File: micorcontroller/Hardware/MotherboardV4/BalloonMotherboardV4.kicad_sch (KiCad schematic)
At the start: 6 parts

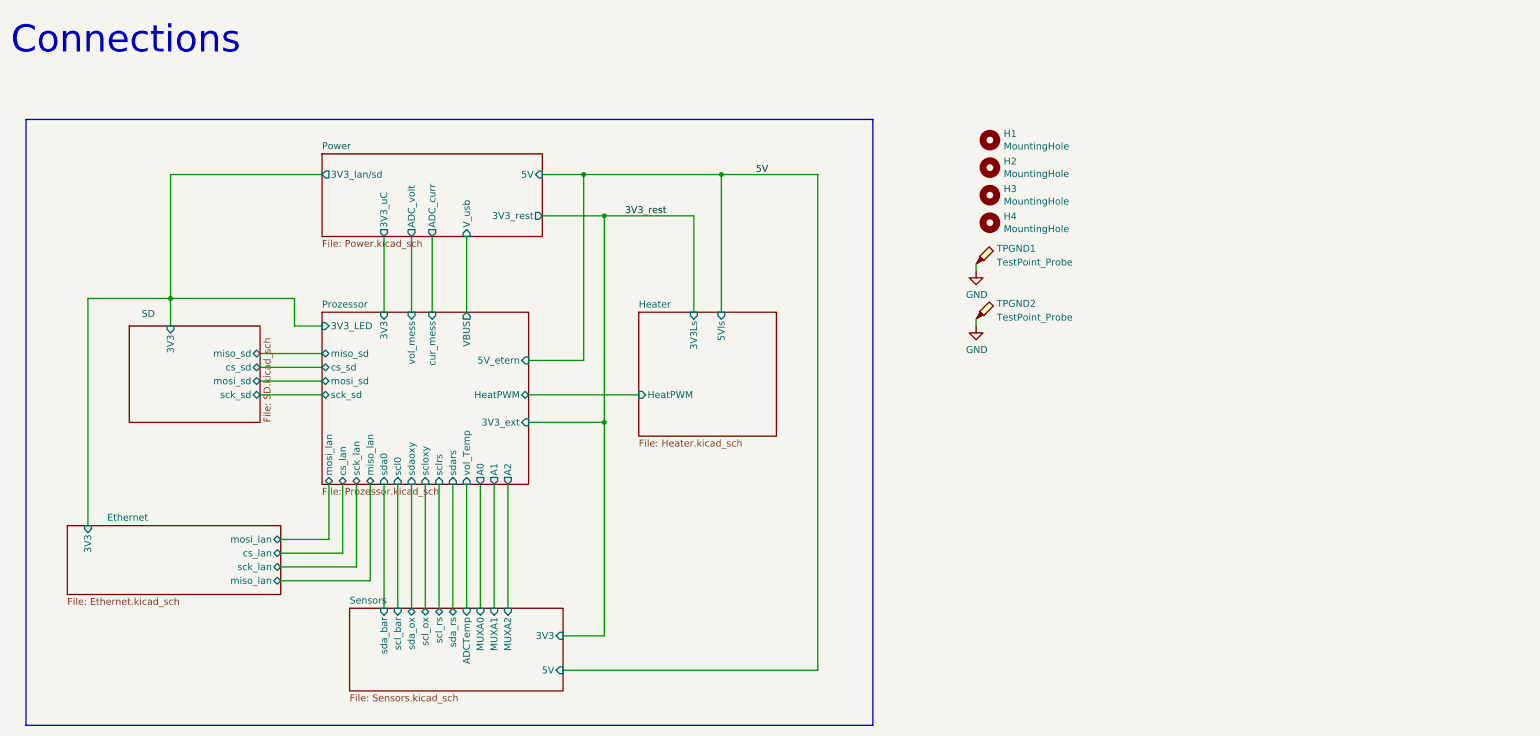
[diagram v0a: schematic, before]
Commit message: added NTC calculation
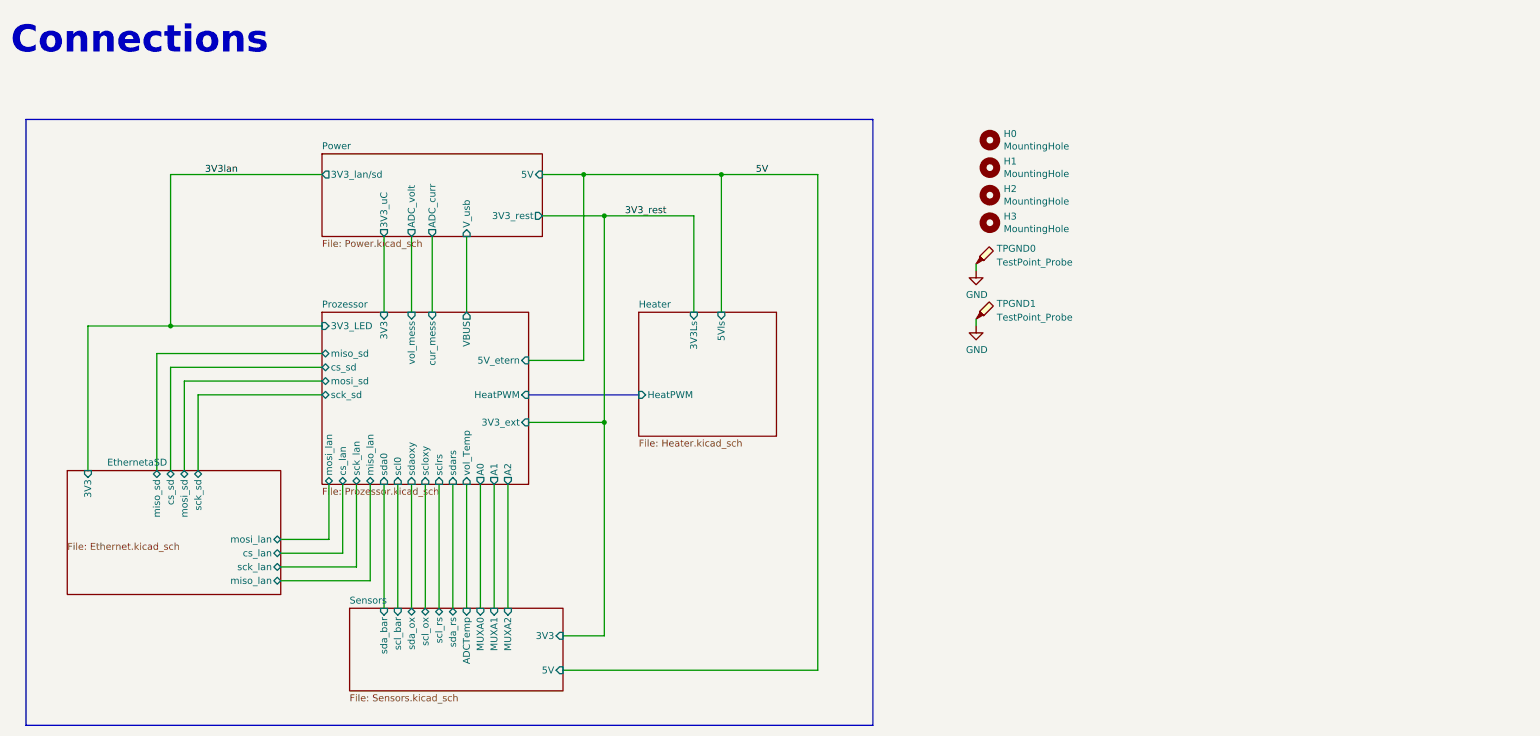
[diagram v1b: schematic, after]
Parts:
- renumbered H1 to H0, H2 to H1, H3 to H2, H4 to H3, TPGND1 to TPGND0, TPGND2 to TPGND1
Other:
- sheet Ethernet renamed EthernetaSD
- removed sheet SD
- sheet EthernetaSD ports: added cs_sd, miso_sd, mosi_sd, sck_sd; removed none

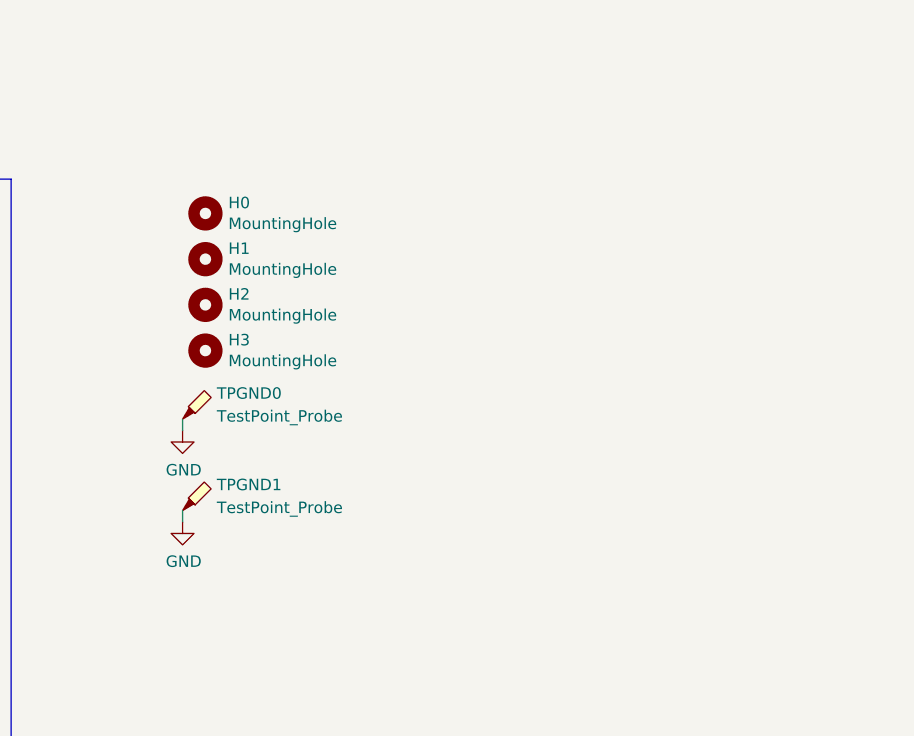
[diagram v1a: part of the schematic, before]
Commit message: added a serial command field for easy debugging
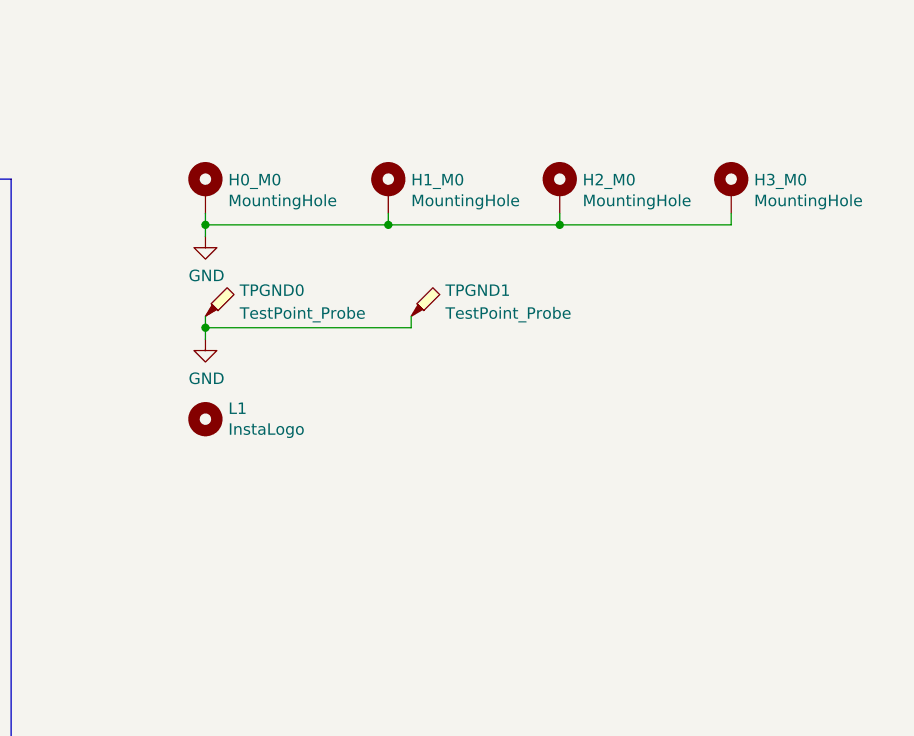
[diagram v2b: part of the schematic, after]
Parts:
- added L1: InstaLogo, SamacSys_Parts:insta, symbol Mechanical:MountingHole
- H0_M0: renamed from H0; symbol Mechanical:MountingHole -> Mechanical:MountingHole_Pad
- H1_M0: renamed from H1; symbol Mechanical:MountingHole -> Mechanical:MountingHole_Pad
- H2_M0: renamed from H2; symbol Mechanical:MountingHole -> Mechanical:MountingHole_Pad
- H3_M0: renamed from H3; symbol Mechanical:MountingHole -> Mechanical:MountingHole_Pad
- TPGND0, TPGND1: now left out of the parts list
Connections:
- net GND: now also H0_M0.1, H1_M0.1, H2_M0.1, H3_M0.1
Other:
- moved on the sheet: TPGND0, TPGND1

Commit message: Switch to header BASED C file system {headache incomming}
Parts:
- renumbered L1 to L0
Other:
- sheet Power ports: added VBUCK; removed none
- sheet Sensors ports: added 3V3uC, BUCK; removed none
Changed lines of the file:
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@@
+	)
+	(junction
+		(at 91.44 66.04)
+		(diameter 0)
+		(color 0 0 0 0)
 	)
 	(junction
@@
 	(wire
 		(pts
+			(xy 120.65 52.07) (xy 167.64 52.07)
+		)
+		(stroke
+			(width 0)
+			(type default)
+		)
+	)
+	(wire
+		(pts
 			(xy 203.2 53.34) (xy 203.2 54.61)
 		)
@@
 	(wire
 		(pts
+			(xy 167.64 52.07) (xy 167.64 135.89)
+		)
+		(stroke
+			(width 0)
+			(type default)
+		)
+	)
+	(wire
+		(pts
 			(xy 57.15 88.9) (xy 80.01 88.9)
 		)
@@
 	(wire
 		(pts
+			(xy 125.73 130.81) (xy 125.73 66.04)
+		)
+		(stroke
+			(width 0)
+			(type default)
+		)
+	)
+	(wire
+		(pts
 			(xy 49.53 81.28) (xy 49.53 102.87)
 		)
@@
 	(wire
 		(pts
+			(xy 91.44 66.04) (xy 91.44 73.66)
+		)
+		(stroke
+			(width 0)
+			(type default)
+		)
+	)
+	(wire
+		(pts
 			(xy 104.14 105.41) (xy 104.14 128.27)
 		)
@@
 	(wire
 		(pts
+			(xy 124.46 130.81) (xy 125.73 130.81)
+		)
+		(stroke
+			(width 0)
+			(type default)
+		)
+	)
+	(wire
+		(pts
 			(xy 118.11 93.98) (xy 132.08 93.98)
 		)
@@
 	(wire
 		(pts
+			(xy 125.73 66.04) (xy 91.44 66.04)
+		)
+		(stroke
+			(width 0)
+			(type default)
+		)
+	)
+	(wire
+		(pts
 			(xy 132.08 55.88) (xy 148.59 55.88)
 		)
@@
 	(wire
 		(pts
+			(xy 167.64 135.89) (xy 124.46 135.89)
+		)
+		(stroke
+			(width 0)
+			(type default)
+		)
+	)
+	(wire
+		(pts
 			(xy 226.06 54.61) (xy 226.06 53.34)
 		)
@@
 	(wire
 		(pts
-			(xy 91.44 59.69) (xy 91.44 73.66)
+			(xy 91.44 59.69) (xy 91.44 66.04)
 		)
 		(stroke
@@
 		(on_board yes)
 		(dnp no)
-		(property "Reference" "L1"
+		(property "Reference" "L0"
 			(at 205.74 63.6016 0)
 			(effects
@@
 			(project "BalloonMotherboardV4"
 				(path "/a70d325c-f83f-4714-a2b6-4ef8919d016e"
-					(reference "L1")
+					(reference "L0")
 					(unit 1)
 				)
@@
 		(on_board yes)
 		(dnp no)
-		(property "Reference" "#PWR00"
+		(property "Reference" "#PWR01"
 			(at 203.2 62.23 0)
 			(effects
@@
 			(project "BalloonMotherboardV4"
 				(path "/a70d325c-f83f-4714-a2b6-4ef8919d016e"
-					(reference "#PWR00")
+					(reference "#PWR01")
 					(unit 1)
 				)
@@
 		(on_board yes)
 		(dnp no)
-		(property "Reference" "#PWR01"
+		(property "Reference" "#PWR00"
 			(at 203.2 50.8 0)
 			(effects
@@
 			(project "BalloonMotherboardV4"
 				(path "/a70d325c-f83f-4714-a2b6-4ef8919d016e"
-					(reference "#PWR01")
+					(reference "#PWR00")
 					(unit 1)
 				)
@@
 			)
 		)
+		(pin "VBUCK" input
+			(at 120.65 52.07 0)
+			(effects
+				(font
+					(size 1.27 1.27)
+				)
+				(justify right)
+			)
+		)
 		(instances
 			(project "BalloonMotherboardV4"
@@
 			(effects
 				(font
+					(size 1.27 1.27)
+				)
+				(justify right)
+			)
+		)
+		(pin "3V3uC" input
+			(at 124.46 130.81 0)
+			(effects
+				(font
+					(size 1.27 1.27)
+				)
+				(justify right)
+			)
+		)
+		(pin "BUCK" input
+			(at 124.46 135.89 0)
+			(effects
+				(font

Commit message: added uplink
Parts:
- H0_M0, H1_M0, H2_M0, H3_M0: symbol Mechanical:MountingHole_Pad -> SymbolsBalloonv4:MountingHole_Pad
- L0: symbol Mechanical:MountingHole -> SymbolsBalloonv4:MountingHole
- TPGND0, TPGND1: symbol Connector:TestPoint_Probe -> SymbolsBalloonv4:TestPoint_Probe
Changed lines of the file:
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@@
 	)
 	(symbol
-		(lib_id "Connector:TestPoint_Probe")
+		(lib_id "SymbolsBalloonv4:TestPoint_Probe")
 		(at 226.06 53.34 0)
 		(unit 1)
@@
 	)
 	(symbol
-		(lib_id "Mechanical:MountingHole_Pad")
+		(lib_id "SymbolsBalloonv4:MountingHole_Pad")
 		(at 261.62 39.37 0)
 		(unit 1)
@@
 	)
 	(symbol
-		(lib_id "Mechanical:MountingHole")
+		(lib_id "SymbolsBalloonv4:MountingHole")
 		(at 203.2 64.77 0)
 		(unit 1)
@@
 	)
 	(symbol
-		(lib_id "power:GND")
+		(lib_id "SymbolsBalloonv4:GND")
 		(at 203.2 55.88 0)
 		(unit 1)
@@
 	)
 	(symbol
-		(lib_id "Mechanical:MountingHole_Pad")
+		(lib_id "SymbolsBalloonv4:MountingHole_Pad")
 		(at 242.57 39.37 0)
 		(unit 1)
@@
 	)
 	(symbol
-		(lib_id "Mechanical:MountingHole_Pad")
+		(lib_id "SymbolsBalloonv4:MountingHole_Pad")
 		(at 203.2 39.37 0)
 		(unit 1)
@@
 	)
 	(symbol
-		(lib_id "power:GND")
+		(lib_id "SymbolsBalloonv4:GND")
 		(at 203.2 44.45 0)
 		(unit 1)
@@
 	)
 	(symbol
-		(lib_id "Connector:TestPoint_Probe")
+		(lib_id "SymbolsBalloonv4:TestPoint_Probe")
 		(at 203.2 53.34 0)
 		(unit 1)
@@
 	)
 	(symbol
-		(lib_id "Mechanical:MountingHole_Pad")
+		(lib_id "SymbolsBalloonv4:MountingHole_Pad")
 		(at 223.52 39.37 0)
 		(unit 1)

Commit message: changed debug to level based debug and started writing driver for FD-OEM Module
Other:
- note added: "Bekannte Designfehler - Input Rush von Buck Converter Condesnsatoren von Heater Condensatoren nicht begrenzt (induktor?) - Pulldown Resistoren bei Voltageshifter zwischen OE und GND und NTCs allgemein fehlen - keine seperate Analog/HF Groundplanes - BAttery Voltage MEasurement befor shunt"
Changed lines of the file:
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@@
+		)
+	)
+	(text "Bekannte Designfehler\n- Input Rush von Buck Converter Condesnsatoren \n		     von Heater Condensatoren\n	nicht begrenzt (induktor?)\n- Pulldown Resistoren bei Voltageshifter zwischen OE und GND\n  und NTCs allgemein fehlen\n- keine seperate Analog/HF Groundplanes\n- BAttery Voltage MEasurement befor shunt"
+		(exclude_from_sim no)
+		(at 185.674 77.724 0)
+		(effects
+			(font
+				(size 2 2)
+				(color 255 255 255 1)
+			)
+			(justify left top)
 		)
 	)
